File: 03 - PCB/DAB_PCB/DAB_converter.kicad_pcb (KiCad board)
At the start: 2 copper layers, 163.5 x 128 mm, 201 parts, among them IC1 UCC27288DR, IC10 INA201AID, IC11 INA201AID, IC12 MCP6241-E_P, IC13 MCP6241-E_P, IC2 UCC27288DR, IC3 UCC27288DR, IC4 UCC27288DR, IC5 UA78L12ACDR, IC6 INA201AID, IC9 INA201AID, J3 N3431-6302RB

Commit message: DRC passed
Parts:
- moved Me1 2.83 mm to (183.5, 37.5)
- moved TP21 0.53 mm to (100.5, 86.5)
- moved Chi2 0.50 mm to (105.0, 83.8)
- moved G*** 0.50 mm to (52.0, 156.5)
- moved TP25 0.50 mm to (100.5, 90.5)
- moved TP6 0.28 mm to (141.0, 88.0)
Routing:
- net 3V3sec: track 178.9 -> 195.9 mm
- net /vs1: track 55.8 -> 70.1 mm
- net /vg4: track 18.8 -> 20.9 mm
- net 12Vsec: track 177.0 -> 178.1 mm
- net /sec+: track 135.5 -> 136.5 mm, vias 7 -> 5
- net /ac-: track 97.5 -> 98.4 mm
- net Net-(IC9-CMP_IN): track 11.0 -> 11.9 mm
- net Net-(IC6-~{RESET}): track 64.2 -> 64.8 mm
- net /PWM2A_ISO: track 100.9 -> 101.5 mm
- net /PWM2B_ISO: track 91.0 -> 91.5 mm
- net GND: vias 15 -> 32

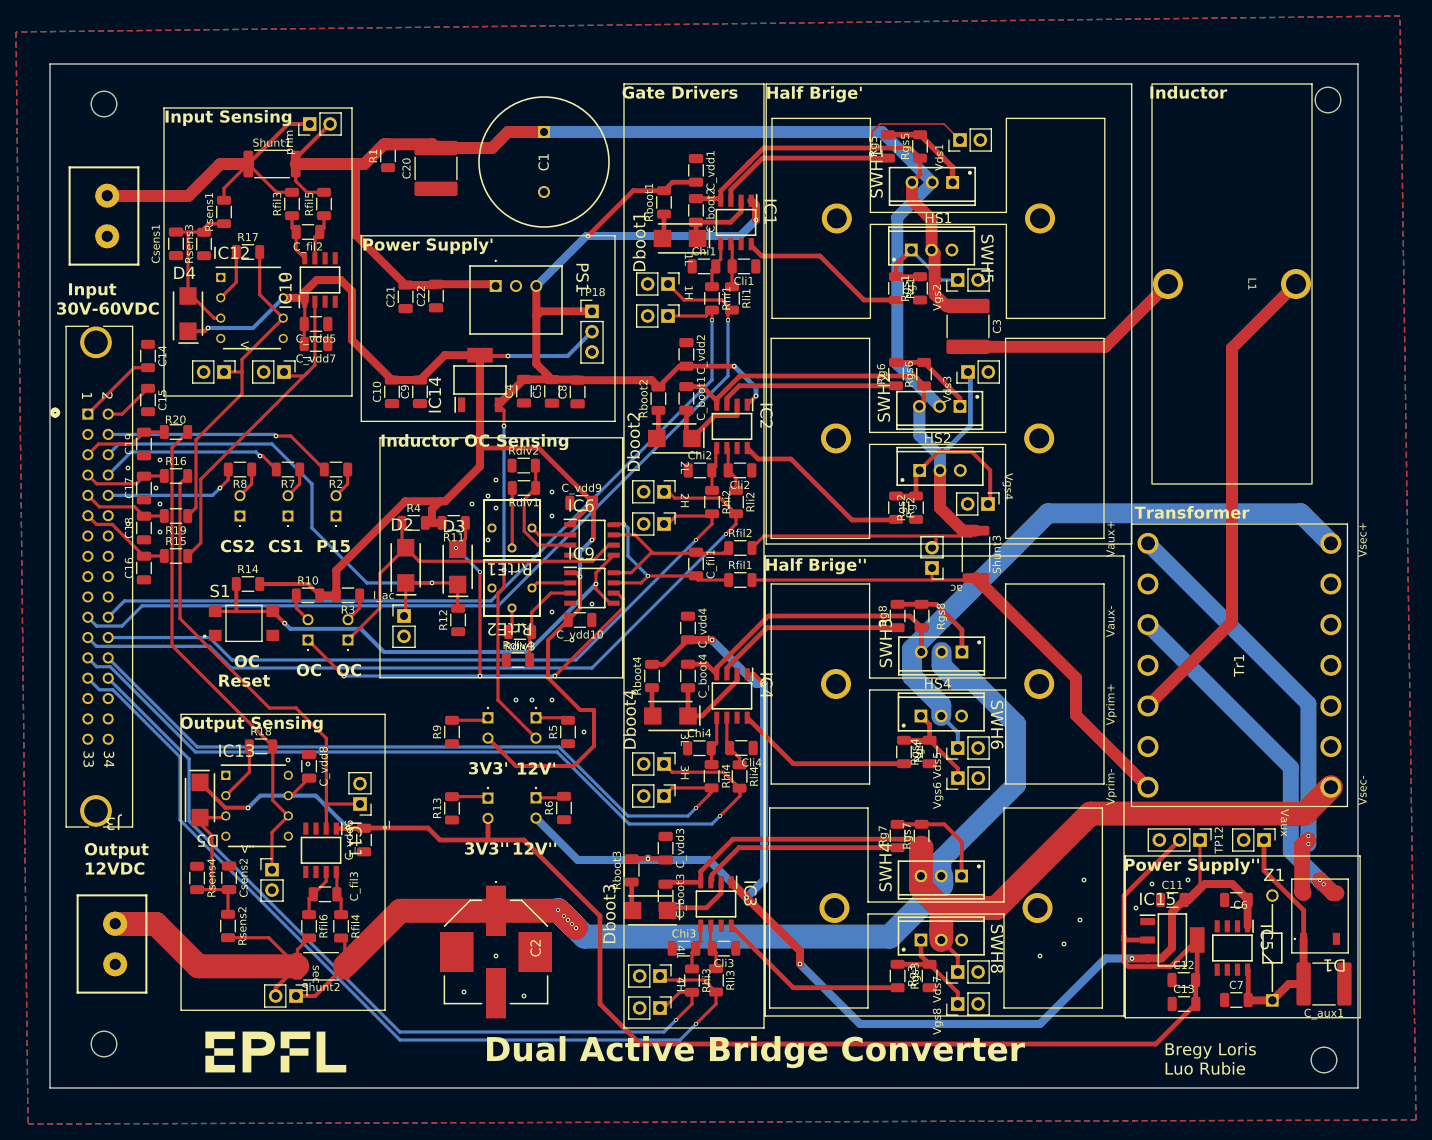
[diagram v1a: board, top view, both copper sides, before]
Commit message: cleaned up silkscreen
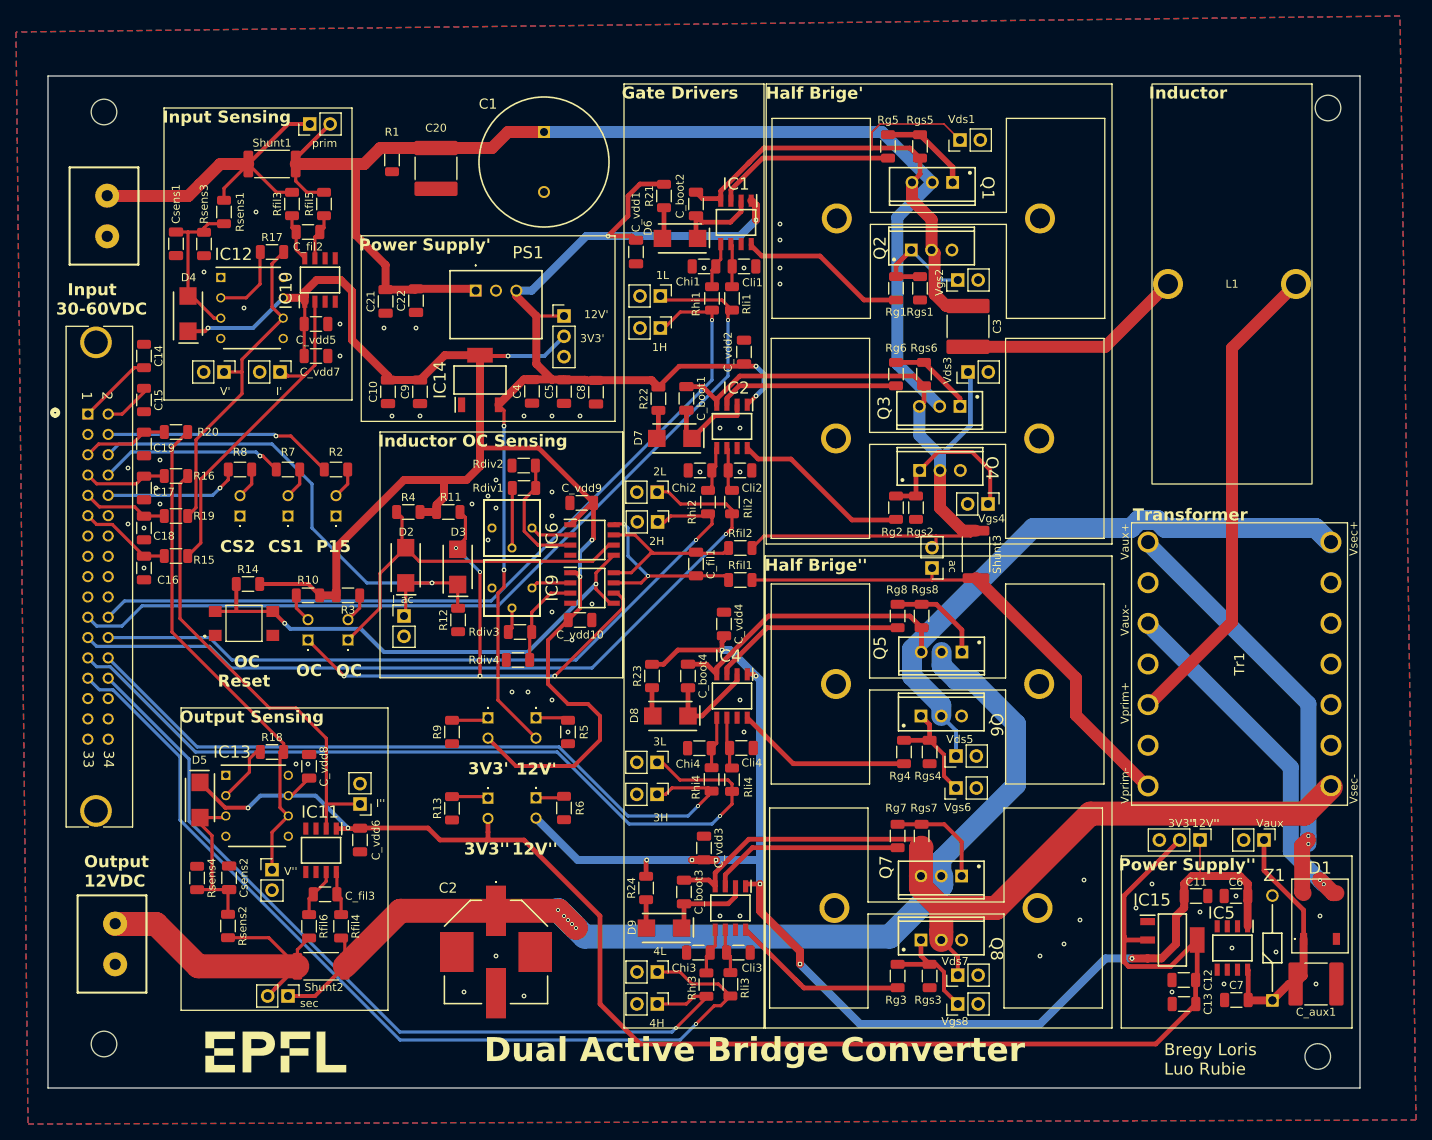
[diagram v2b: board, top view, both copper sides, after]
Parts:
- moved C_vdd1 12.7 mm to (97.0, 56.5), turned to 90 degrees
- moved C_vdd2 7.21 mm to (110.5, 69.0)
- moved C_vdd3 4.80 mm to (105.5, 131.0)
- moved C_vdd4 4.53 mm to (108.0, 103.0)
- moved TP18 3.55 mm to (88.0, 64.5)
- moved R17 3.00 mm to (51.5, 56.5)
- moved C11 2.99 mm to (167.0, 137.0), turned to 180 degrees
- moved R24 2.84 mm to (98.3, 136.0)
- moved D9 2.80 mm to (100.5, 141.0)
- moved C21 2.57 mm to (65.7, 62.7)
- moved C22 2.57 mm to (69.5, 62.6)
- moved PS1 2.57 mm to (77.0, 61.3)
- moved C_boot3 2.35 mm to (103.0, 136.5)
- moved C8 2.30 mm to (92.0, 74.0)
- moved Chi3 1.87 mm to (104.8, 144.1)
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- renumbered Dboot1 to D6, Dboot2 to D7, Dboot4 to D8, Dboot3 to D9, SWH1 to Q1, SWH5 to Q2, SWH2 to Q3, SWH7 to Q4, SWH3 to Q5, SWH6 to Q6, SWH4 to Q7, SWH8 to Q8, Rboot1 to R21, Rboot2 to R22, Rboot4 to R23, Rboot3 to R24
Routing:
- net 12Vsec: track 178.1 -> 170.9 mm, vias 6 -> 8
- net /PWM4A_ISO: track 113.1 -> 116.3 mm
- net /PWM4B_ISO: track 103.6 -> 106.8 mm
- net Net-(IC12-VIN-): track 6.53 -> 9.64 mm
- net Net-(D9-K): track 9.05 -> 11.2 mm
- net Net-(D3-A): track 68.5 -> 70.1 mm
- net Net-(D2-A): track 45.4 -> 47.0 mm
- net /PWM1B_ISO: track 102.3 -> 103.9 mm
- net /vs7: track 108.0 -> 106.7 mm
- net Net-(IC3-LO): track 24.0 -> 22.7 mm
- net Net-(IC3-HO): track 25.6 -> 24.4 mm
- net /vg6: track 12.9 -> 14.0 mm
- net Net-(D6-K): track 9.65 -> 10.8 mm
- net /sec+: track 136.5 -> 137.5 mm
- net /prim-: track 158.4 -> 157.5 mm
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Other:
- board size 163.5 x 128 mm -> 164 x 126.5 mm
- board text added: "Input 30-60VDC"
- board text removed: "Input 30V-60VDC"

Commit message: added ground vias
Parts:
- moved R14 1.82 mm to (47.5, 99.5)
- moved S1 1.82 mm to (47.0, 104.4)
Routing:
- net /V'': track 63.1 -> 67.5 mm
- net /I'': track 59.2 -> 62.8 mm
- net 3V3pri: track 206.2 -> 207.8 mm
- net Net-(IC6-~{RESET}): track 64.7 -> 65.6 mm
- net GND: vias 66 -> 168
